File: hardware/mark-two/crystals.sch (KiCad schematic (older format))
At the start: 20 parts, among them U2 MX6UL-VM, Y1 24MHz, Y2 32.768kHz

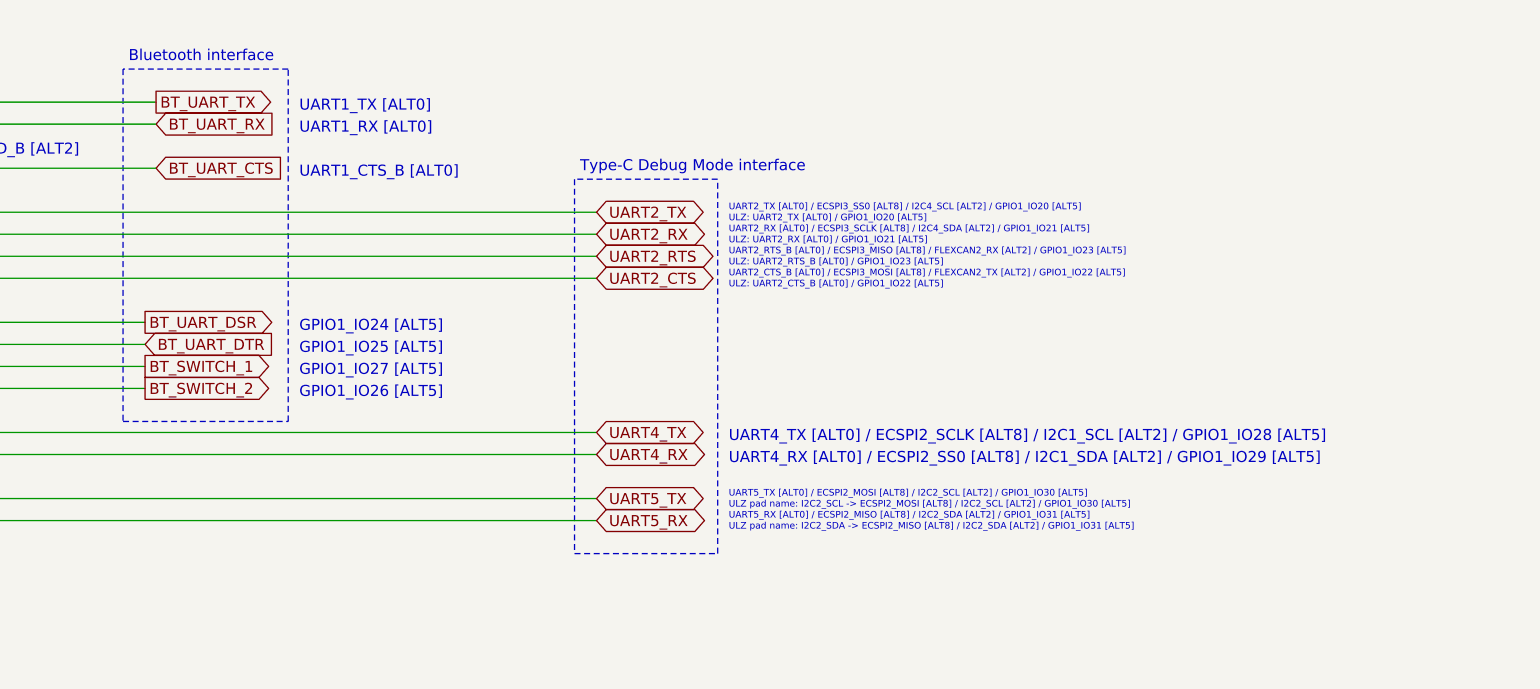
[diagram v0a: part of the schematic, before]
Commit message: add USB armory Mk II rev. γ
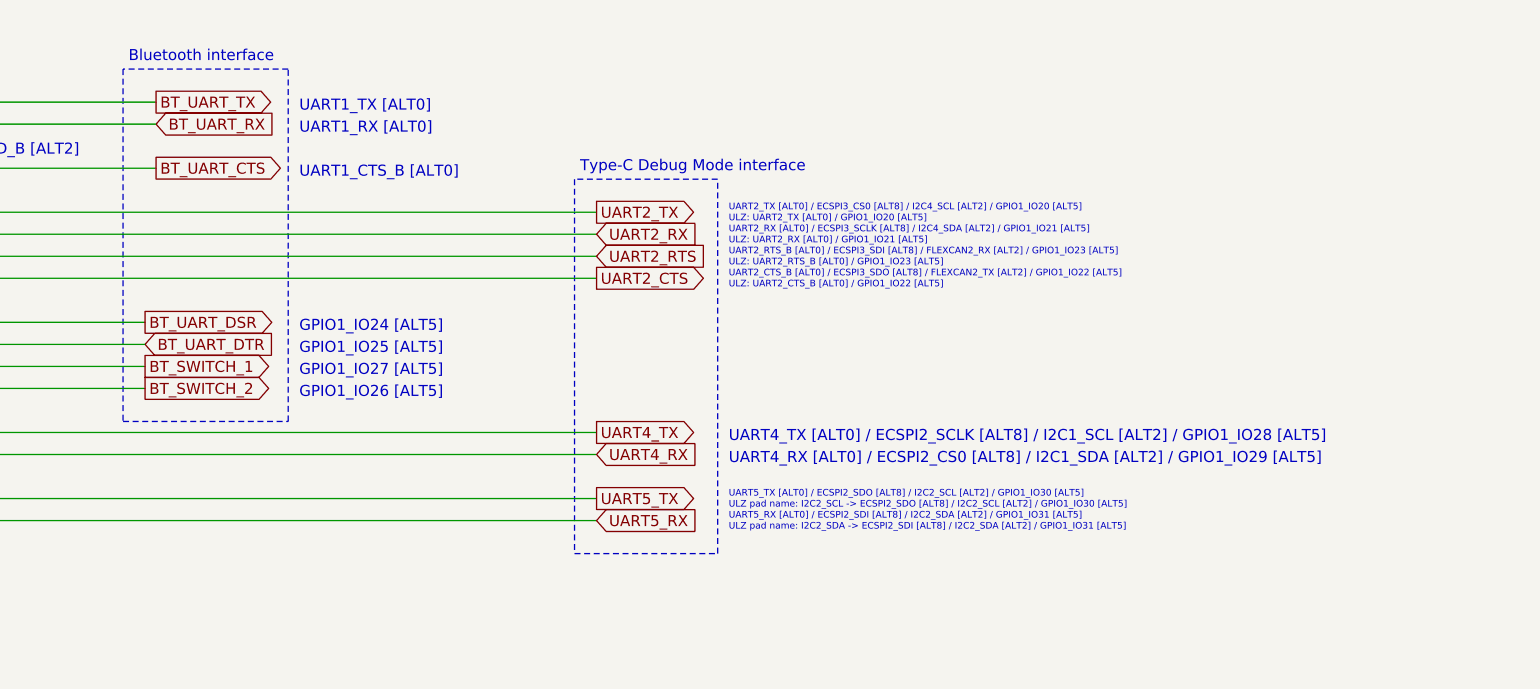
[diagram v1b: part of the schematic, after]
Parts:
- C30, C31: Alternative PN (none) -> GRM0335C1H180GA01D
- U2: Mfg PN (none) -> MCIMX6Z0DVM09AB
- Y1: Alternative PN (none) -> TSX-3225 24.0000MF15X-AC6
- Y2: Alternative PN (none) -> CM7V-T1A-32.768kHz-12.5pF-20PPM-TA-QA
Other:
- note added: "UART2_CTS_B [ALT0] / ECSPI3_SDO [ALT8] / FLEXCAN2_TX [ALT2] / GPIO1_IO22 [ALT5]"
- note added: "UART2_RTS_B [ALT0] / ECSPI3_SDI [ALT8] / FLEXCAN2_RX [ALT2] / GPIO1_IO23 [ALT5]"
- note added: "UART2_TX [ALT0] / ECSPI3_CS0 [ALT8] / I2C4_SCL [ALT2] / GPIO1_IO20 [ALT5]"
- note added: "UART4_RX [ALT0] / ECSPI2_CS0 [ALT8] / I2C1_SDA [ALT2] / GPIO1_IO29 [ALT5]"
- note added: "UART5_RX [ALT0] / ECSPI2_SDI [ALT8] / I2C2_SDA [ALT2] / GPIO1_IO31 [ALT5]"
- note added: "UART5_TX [ALT0] / ECSPI2_SDO [ALT8] / I2C2_SCL [ALT2] / GPIO1_IO30 [ALT5]"
- note added: "ULZ pad name: I2C2_SCL -> ECSPI2_SDO [ALT8] / I2C2_SCL [ALT2] / GPIO1_IO30 [ALT5]"
- note added: "ULZ pad name: I2C2_SDA -> ECSPI2_SDI [ALT8] / I2C2_SDA [ALT2] / GPIO1_IO31 [ALT5]"
- note removed: "UART2_CTS_B [ALT0] / ECSPI3_MOSI [ALT8] / FLEXCAN2_TX [ALT2] / GPIO1_IO22 [ALT5]"
- note removed: "UART2_RTS_B [ALT0] / ECSPI3_MISO [ALT8] / FLEXCAN2_RX [ALT2] / GPIO1_IO23 [ALT5]"
- note removed: "UART2_TX [ALT0] / ECSPI3_SS0 [ALT8] / I2C4_SCL [ALT2] / GPIO1_IO20 [ALT5]"
- note removed: "UART4_RX [ALT0] / ECSPI2_SS0 [ALT8] / I2C1_SDA [ALT2] / GPIO1_IO29 [ALT5]"
- note removed: "UART5_RX [ALT0] / ECSPI2_MISO [ALT8] / I2C2_SDA [ALT2] / GPIO1_IO31 [ALT5]"
- note removed: "UART5_TX [ALT0] / ECSPI2_MOSI [ALT8] / I2C2_SCL [ALT2] / GPIO1_IO30 [ALT5]"
- note removed: "ULZ pad name: I2C2_SCL -> ECSPI2_MOSI [ALT8] / I2C2_SCL [ALT2] / GPIO1_IO30 [ALT5]"
- note removed: "ULZ pad name: I2C2_SDA -> ECSPI2_MISO [ALT8] / I2C2_SDA [ALT2] / GPIO1_IO31 [ALT5]"
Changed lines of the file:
@@
 EESchema Schematic File Version 4
-LIBS:armory-cache
 EELAYER 30 0
 EELAYER END
@@
 encoding utf-8
 Sheet 2 13
-Title "USB ARMORY"
-Date "2019-06-25"
-Rev "MARK II"
+Title "USB armory Mk II"
+Date "2021-02-18"
+Rev "γ"
 Comp "F-Secure"
-Comment1 "Copyright © 2019 F-Secure"
-Comment2 "License: CERN OHL v1.2"
-Comment3 "https://github.com/inversepath/usbarmory"
+Comment1 "Copyright © F-Secure Corporation"
+Comment2 "License: CERN-OHL-S"
+Comment3 "https://github.com/f-secure-foundry/usbarmory"
 Comment4 ""
 $EndDescr
@@
 F 2 "armory-kicad:SOT1534-2" H 7685 1665 60  0001 C CNN
 F 3 "https://www.nxp.com/docs/en/data-sheet/IMX6ULCEC.pdf" H 7685 1665 60  0001 C CNN
+F 4 "MCIMX6Z0DVM09AB" H 7175 2825 50  0001 C CNN "Mfg PN"
 	11   7175 2825
 	1    0    0    -1
@@
 F 7 "Mouser" H 4475 6675 50  0001 C CNN "Supplier"
 F 8 "428-200458-MG01" H 4475 6675 50  0001 C CNN "Supplier PN"
+F 9 "CM7V-T1A-32.768kHz-12.5pF-20PPM-TA-QA" H 4475 6675 50  0001 C CNN "Alternative PN"
 	1    4475 6675
 	1    0    0    -1
@@
 F 9 "0201" H 4225 7075 30  0000 C CNN "FP"
 F 10 "50V/5%" H 4325 6925 30  0000 C CNN "Rating"
+F 11 "GRM0335C1H180GA01D" H 4225 7075 50  0001 C CNN "Alternative PN"
 	1    4225 7075
 	1    0    0    -1
@@
 Text GLabel 10125 5425 2    50   Input ~ 0
 BT_UART_RX
-Text GLabel 10125 5625 2    50   Input ~ 0
+Text GLabel 10125 5625 2    50   Output ~ 0
 BT_UART_CTS
 Wire Wire Line
@@
 F 9 "0201" H 4725 7075 30  0000 C CNN "FP"
 F 10 "50V/5%" H 4825 6925 30  0000 C CNN "Rating"
+F 11 "GRM0335C1H180GA01D" H 4725 7075 50  0001 C CNN "Alternative PN"
 	1    4725 7075
 	1    0    0    -1
@@
 F 7 "Digikey" H 3375 5725 50  0001 C CNN "Supplier"
 F 8 "SER3635TR-ND" H 3375 5725 50  0001 C CNN "Supplier PN"
+F 9 "TSX-3225 24.0000MF15X-AC6" H 3375 5725 50  0001 C CNN "Alternative PN"
 	1    3375 5725
 	-1   0    0    1
@@
 	12025 5675 12025 7375
 Text Notes 12725 7275 0    30   ~ 0
-ULZ pad name: I2C2_SDA -> ECSPI2_MISO [ALT8] / I2C2_SDA [ALT2] / GPIO1_IO31 [ALT5]
+ULZ pad name: I2C2_SDA -> ECSPI2_SDI [ALT8] / I2C2_SDA [ALT2] / GPIO1_IO31 [ALT5]
 Text Notes 12725 7175 0    30   ~ 0
-ULZ pad name: I2C2_SCL -> ECSPI2_MOSI [ALT8] / I2C2_SCL [ALT2] / GPIO1_IO30 [ALT5]
+ULZ pad name: I2C2_SCL -> ECSPI2_SDO [ALT8] / I2C2_SCL [ALT2] / GPIO1_IO30 [ALT5]
 Text Notes 12725 6875 0    50   ~ 0
 UART4_TX [ALT0] / ECSPI2_SCLK [ALT8] / I2C1_SCL [ALT2] / GPIO1_IO28 [ALT5]
@@
 Text Notes 12050 5650 0    50   ~ 0
 Type-C Debug Mode interface
-Text GLabel 12125 7125 2    50   BiDi ~ 0
+Text GLabel 12125 7125 2    50   Output ~ 0
 UART5_TX
-Text GLabel 12125 7225 2    50   BiDi ~ 0
+Text GLabel 12125 7225 2    50   Input ~ 0
 UART5_RX
-Text GLabel 12125 6925 2    50   BiDi ~ 0
+Text GLabel 12125 6925 2    50   Input ~ 0
 UART4_RX
-Text GLabel 12125 6825 2    50   BiDi ~ 0
+Text GLabel 12125 6825 2    50   Output ~ 0
 UART4_TX
-Text GLabel 12125 6025 2    50   BiDi ~ 0
+Text GLabel 12125 6025 2    50   Input ~ 0
 UART2_RTS
-Text GLabel 12125 6125 2    50   BiDi ~ 0
+Text GLabel 12125 6125 2    50   Output ~ 0
 UART2_CTS
-Text GLabel 12125 5925 2    50   BiDi ~ 0
+Text GLabel 12125 5925 2    50   Input ~ 0
 UART2_RX
-Text GLabel 12125 5825 2    50   BiDi ~ 0
+Text GLabel 12125 5825 2    50   Output ~ 0
 UART2_TX
 Text Notes 12725 7225 0    30   ~ 0
-UART5_RX [ALT0] / ECSPI2_MISO [ALT8] / I2C2_SDA [ALT2] / GPIO1_IO31 [ALT5]
+UART5_RX [ALT0] / ECSPI2_SDI [ALT8] / I2C2_SDA [ALT2] / GPIO1_IO31 [ALT5]
 Text Notes 12725 7125 0    30   ~ 0
-UART5_TX [ALT0] / ECSPI2_MOSI [ALT8] / I2C2_SCL [ALT2] / GPIO1_IO30 [ALT5]
+UART5_TX [ALT0] / ECSPI2_SDO [ALT8] / I2C2_SCL [ALT2] / GPIO1_IO30 [ALT5]
 Text Notes 12725 6975 0    50   ~ 0
-UART4_RX [ALT0] / ECSPI2_SS0 [ALT8] / I2C1_SDA [ALT2] / GPIO1_IO29 [ALT5]
+UART4_RX [ALT0] / ECSPI2_CS0 [ALT8] / I2C1_SDA [ALT2] / GPIO1_IO29 [ALT5]
 Text Notes 12725 6025 0    30   ~ 0
-UART2_RTS_B [ALT0] / ECSPI3_MISO [ALT8] / FLEXCAN2_RX [ALT2] / GPIO1_IO23 [ALT5]
+UART2_RTS_B [ALT0] / ECSPI3_SDI [ALT8] / FLEXCAN2_RX [ALT2] / GPIO1_IO23 [ALT5]
 Text Notes 12725 6125 0    30   ~ 0
-UART2_CTS_B [ALT0] / ECSPI3_MOSI [ALT8] / FLEXCAN2_TX [ALT2] / GPIO1_IO22 [ALT5]
+UART2_CTS_B [ALT0] / ECSPI3_SDO [ALT8] / FLEXCAN2_TX [ALT2] / GPIO1_IO22 [ALT5]
 Text Notes 12725 5925 0    30   ~ 0
 UART2_RX [ALT0] / ECSPI3_SCLK [ALT8] / I2C4_SDA [ALT2] / GPIO1_IO21 [ALT5]
 Text Notes 12725 5825 0    30   ~ 0
-UART2_TX [ALT0] / ECSPI3_SS0 [ALT8] / I2C4_SCL [ALT2] / GPIO1_IO20 [ALT5]
+UART2_TX [ALT0] / ECSPI3_CS0 [ALT8] / I2C4_SCL [ALT2] / GPIO1_IO20 [ALT5]
 Wire Wire Line
 	12125 6025 8475 6025
